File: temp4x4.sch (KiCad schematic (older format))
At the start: 15 parts, among them J1 NUCLEO_CN6_1-6, J2 NUCLEO_CN5_10-1, U1 LP5907MFX-3.3_NOPB, U2 ADS124S08IPBS

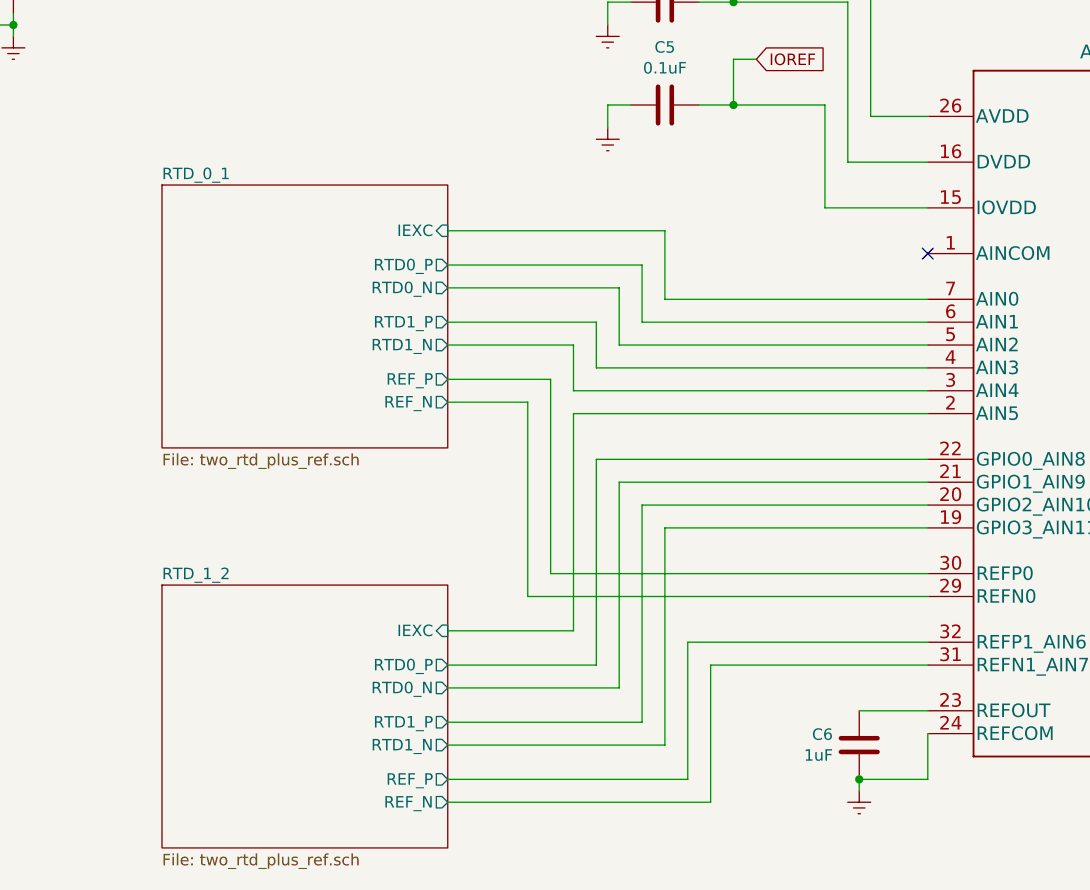
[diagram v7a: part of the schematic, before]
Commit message: changed pin connections to simplify the layout
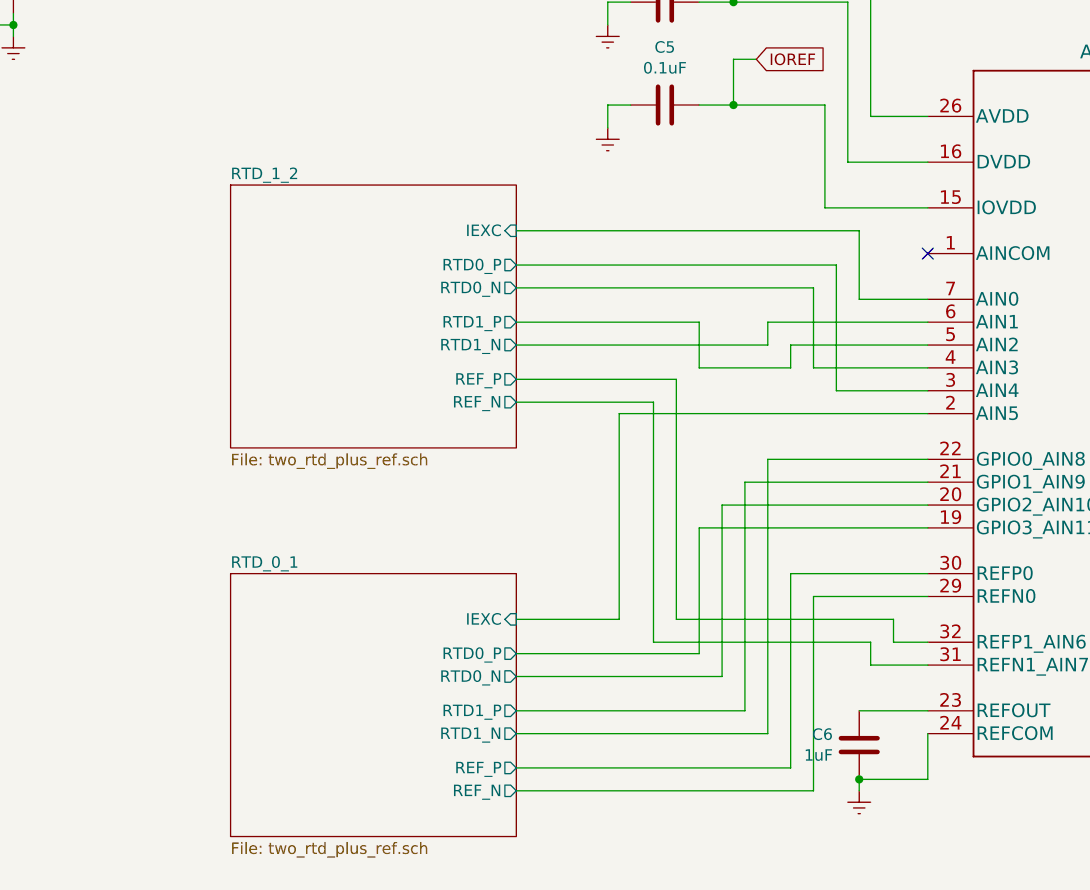
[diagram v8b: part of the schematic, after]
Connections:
- net RTD_0_1/IEXC: now also U2.2 (AIN5); no longer U2.7 (AIN0)
- net RTD_0_1/RTD0_N: now also U2.20 (GPIO2_AIN10); no longer U2.5 (AIN2)
- net RTD_0_1/RTD0_P: now also U2.19 (GPIO3_AIN11); no longer U2.6 (AIN1)
- net RTD_0_1/RTD1_N: now also U2.22 (GPIO0_AIN8); no longer U2.3 (AIN4)
- net RTD_0_1/RTD1_P: now also U2.21 (GPIO1_AIN9); no longer U2.4 (AIN3)
- net RTD_1_2/IEXC: now also U2.7 (AIN0); no longer U2.2 (AIN5)
- net RTD_1_2/RTD0_N: now also U2.4 (AIN3); no longer U2.21 (GPIO1_AIN9)
- net RTD_1_2/RTD0_P: now also U2.3 (AIN4); no longer U2.22 (GPIO0_AIN8)
- net RTD_1_2/RTD1_N: now also U2.6 (AIN1); no longer U2.19 (GPIO3_AIN11)
- net RTD_1_2/RTD1_P: now also U2.5 (AIN2); no longer U2.20 (GPIO2_AIN10)
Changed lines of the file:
@@
 Wire Wire Line
 	5600 1550 5600 1650
-$Comp
-L ADS124S08IPBS:ADS124S08IPBS U2
-U 1 1 5EC39B81
-P 8000 3350
-F 0 "U2" H 8000 5038 60  0000 C CNN
-F 1 "ADS124S08IPBS" H 8000 4932 60  0000 C CNN
-F 2 "Package_QFP:LQFP-32_5x5mm_P0.5mm" H 8000 3290 60  0001 C CNN
-F 3 "" H 8000 3350 60  0000 C CNN
-	1    8000 3350
-	1    0    0    -1
-$EndComp
 Wire Wire Line
 	9200 3250 9200 4050
@@
 IOREF
 $Sheet
-S 3650 2350 1250 1150
+S 3950 4050 1250 1150
 U 5EC374D6
 F0 "RTD_0_1" 50
 F1 "two_rtd_plus_ref.sch" 50
-F2 "IEXC" I R 4900 2550 50
-F3 "RTD0_P" O R 4900 2700 50
-F4 "RTD0_N" O R 4900 2800 50
-F5 "RTD1_P" O R 4900 2950 50
-F6 "RTD1_N" O R 4900 3050 50
-F7 "REF_P" O R 4900 3200 50
-F8 "REF_N" O R 4900 3300 50
+F2 "IEXC" I R 5200 4250 50
+F3 "RTD0_P" O R 5200 4400 50
+F4 "RTD0_N" O R 5200 4500 50
+F5 "RTD1_P" O R 5200 4650 50
+F6 "RTD1_N" O R 5200 4750 50
+F7 "REF_P" O R 5200 4900 50
+F8 "REF_N" O R 5200 5000 50
 $EndSheet
 Wire Wire Line
@@
 NoConn ~ 7000 2650
 $Sheet
-S 3650 4100 1250 1150
+S 3950 2350 1250 1150
 U 5ED0B429
 F0 "RTD_1_2" 50
 F1 "two_rtd_plus_ref.sch" 50
-F2 "IEXC" I R 4900 4300 50
-F3 "RTD0_P" O R 4900 4450 50
-F4 "RTD0_N" O R 4900 4550 50
-F5 "RTD1_P" O R 4900 4700 50
-F6 "RTD1_N" O R 4900 4800 50
-F7 "REF_P" O R 4900 4950 50
-F8 "REF_N" O R 4900 5050 50
+F2 "IEXC" I R 5200 2550 50
+F3 "RTD0_P" O R 5200 2700 50
+F4 "RTD0_N" O R 5200 2800 50
+F5 "RTD1_P" O R 5200 2950 50
+F6 "RTD1_N" O R 5200 3050 50
+F7 "REF_P" O R 5200 3200 50
+F8 "REF_N" O R 5200 3300 50
 $EndSheet
-Wire Wire Line
-	4900 2550 5850 2550
-Wire Wire Line
-	5850 2550 5850 2850
-Wire Wire Line
-	5850 2850 7000 2850
-Wire Wire Line
-	7000 2950 5750 2950
-Wire Wire Line
-	5750 2950 5750 2700
-Wire Wire Line
-	5750 2700 4900 2700
-Wire Wire Line
-	7000 3050 5650 3050
-Wire Wire Line
-	5650 3050 5650 2800
-Wire Wire Line
-	5650 2800 4900 2800
-Wire Wire Line
-	7000 3150 5550 3150
-Wire Wire Line
-	5550 3150 5550 2950
-Wire Wire Line
-	5550 2950 4900 2950
-Wire Wire Line
-	7000 3250 5450 3250
-Wire Wire Line
-	5450 3250 5450 3050
-Wire Wire Line
-	5450 3050 4900 3050
-Wire Wire Line
-	7000 4050 5350 4050
-Wire Wire Line
-	5350 4050 5350 3200
-Wire Wire Line
-	5350 3200 4900 3200
-Wire Wire Line
-	7000 4150 5250 4150
-Wire Wire Line
-	5250 4150 5250 3300
-Wire Wire Line
-	5250 3300 4900 3300
-Wire Wire Line
-	7000 3350 5450 3350
-Wire Wire Line
-	5450 3350 5450 4300
-Wire Wire Line
-	5450 4300 4900 4300
-Wire Wire Line
-	7000 3550 5550 3550
-Wire Wire Line
-	5550 3550 5550 4450
-Wire Wire Line
-	5550 4450 4900 4450
-Wire Wire Line
-	7000 3650 5650 3650
-Wire Wire Line
-	5650 3650 5650 4550
-Wire Wire Line
-	5650 4550 4900 4550
-Wire Wire Line
-	7000 3750 5750 3750
-Wire Wire Line
-	5750 3750 5750 4700
-Wire Wire Line
-	5750 4700 4900 4700
-Wire Wire Line
-	7000 3850 5850 3850
-Wire Wire Line
-	5850 3850 5850 4800
-Wire Wire Line
-	5850 4800 4900 4800
-Wire Wire Line
-	7000 4350 5950 4350
-Wire Wire Line
-	5950 4350 5950 4950
-Wire Wire Line
-	5950 4950 4900 4950
-Wire Wire Line
-	7000 4450 6050 4450
-Wire Wire Line
-	6050 4450 6050 5050
-Wire Wire Line
-	6050 5050 4900 5050
 $Comp
 L power:Earth #PWR06
@@
 NoConn ~ 1550 3950
 NoConn ~ 1550 3850
+Wire Wire Line
+	5200 3200 5900 3200
+Wire Wire Line
+	5200 3300 5800 3300
+Wire Wire Line
+	5650 4250 5200 4250
+Wire Wire Line
+	6000 4400 5200 4400
+Wire Wire Line
+	6100 4500 5200 4500
+Wire Wire Line
+	6200 4650 5200 4650
+Wire Wire Line
+	6300 4750 5200 4750
+Wire Wire Line
+	6400 4900 5200 4900
+Wire Wire Line
+	6500 5000 5200 5000
+Wire Wire Line
+	6700 2550 6700 2850
+Wire Wire Line
+	6700 2850 7000 2850
+Wire Wire Line
+	5200 2550 6700 2550
+Wire Wire Line
+	5200 2700 6600 2700
+Wire Wire Line
+	5200 2800 6500 2800
+Wire Wire Line
+	7000 3350 5650 3350
+Wire Wire Line
+	5650 3350 5650 4250
+$Comp
+L ADS124S08IPBS:ADS124S08IPBS U2
+U 1 1 5EC39B81
+P 8000 3350
+F 0 "U2" H 8000 5038 60  0000 C CNN
+F 1 "ADS124S08IPBS" H 8000 4932 60  0000 C CNN
+F 2 "Package_QFP:LQFP-32_5x5mm_P0.5mm" H 8000 3290 60  0001 C CNN
+F 3 "" H 8000 3350 60  0000 C CNN
+	1    8000 3350
+	1    0    0    -1
+$EndComp
+Wire Wire Line
+	6600 3250 7000 3250
+Wire Wire Line
+	6600 2700 6600 3250
+Wire Wire Line
+	6500 3150 7000 3150
+Wire Wire Line
+	6500 2800 6500 3150
+Wire Wire Line
+	5200 2950 6000 2950
+Wire Wire Line
+	6400 3050 7000 3050
+Wire Wire Line
+	5200 3050 6300 3050
+Wire Wire Line
+	6300 3050 6300 2950
+Wire Wire Line
+	6300 2950 7000 2950
+Wire Wire Line
+	6000 2950 6000 3150
+Wire Wire Line
+	6000 3150 6400 3150
+Wire Wire Line
+	6400 3150 6400 3050
+Wire Wire Line
+	6200 3650 7000 3650
+Wire Wire Line
+	6200 3650 6200 4650
+Wire Wire Line
+	6300 4750 6300 3550
+Wire Wire Line
+	6300 3550 7000 3550
+Wire Wire Line
+	6000 4400 6000 3850
+Wire Wire Line
+	6000 3850 7000 3850
+Wire Wire Line
+	6100 4500 6100 3750
+Wire Wire Line
+	6100 3750 7000 3750
+Wire Wire Line
+	6400 4050 7000 4050
+Wire Wire Line
+	6400 4050 6400 4900
+Wire Wire Line
+	6500 4150 7000 4150
+Wire Wire Line
+	6500 4150 6500 5000
+Wire Wire Line
+	5900 4250 6850 4250
+Wire Wire Line
+	6850 4250 6850 4350
+Wire Wire Line
+	6850 4350 7000 4350
+Wire Wire Line
+	5900 3200 5900 4250
+Wire Wire Line
+	5800 4350 6750 4350
+Wire Wire Line
+	6750 4350 6750 4450
+Wire Wire Line
+	6750 4450 7000 4450
+Wire Wire Line
+	5800 3300 5800 4350
 $EndSCHEMATC
